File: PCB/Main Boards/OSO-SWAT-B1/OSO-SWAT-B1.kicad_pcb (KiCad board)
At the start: 2 copper layers, 24.4 x 24.4 mm, 37 parts, among them J1 OSO_SWD, U1 ATSAML22J18A-MUT, U2 MIC5365-3.3YC5-TR, X1 32.768 kHz, 12.5 pF

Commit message: as sent to JLCPCB 10/12
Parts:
- R1: value TBD -> 1K

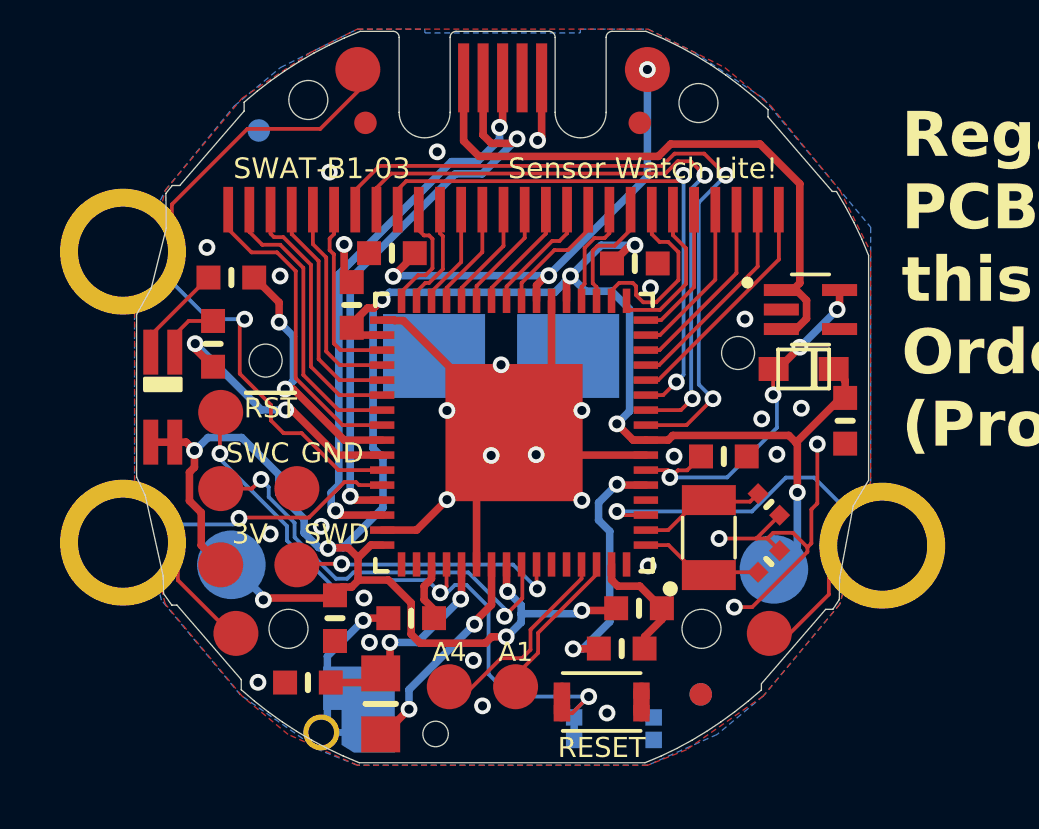
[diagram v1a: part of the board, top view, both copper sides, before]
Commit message: DFM changes for JLC release
- Change small value capacitors to 0.1uF
- Fix footprint / library associations
- Change test points to discrete footprints
- Use smaller LED
- Change to DFN-6 LDO
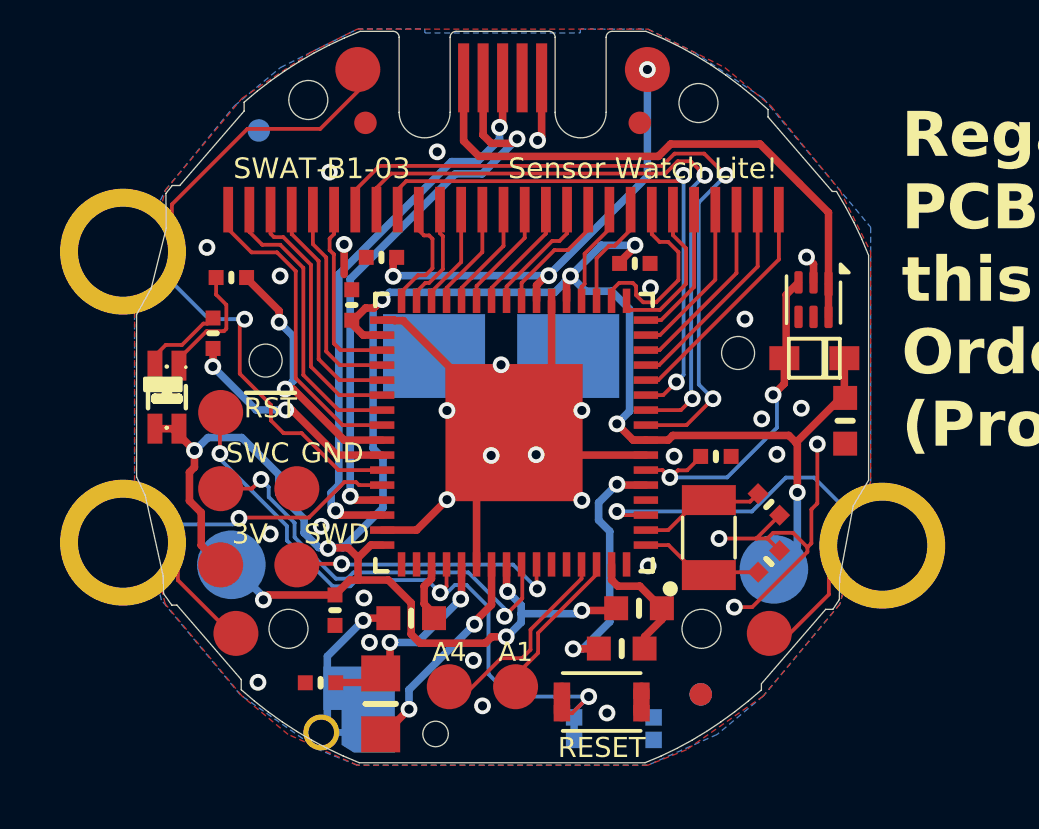
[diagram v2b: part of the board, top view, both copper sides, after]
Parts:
- removed J1: OSO_SWD, OSO-SWD:OSO_SWD_2x3
- removed U$5: , OSO-SWAT-A1-05:OSO_BEAR_250X360MIL_1000DPI
- removed U$6: , OSO-SWAT-A1-05:OSO_WORDMARK_ONELINE_350MIL_1000DPI
- removed U2: MIC5365-3.3YC5-TR, OSO-SWAT-A1-05:SOT65P210X110-5N
- added TP11: TestPoint, TestPoint:TestPoint_Pad_D1.5mm, F.Cu at (5.57, 13.3)
- added TP2: TestPoint, TestPoint:TestPoint_Pad_D1.5mm, F.Cu at (8.11, 18.4)
- added TP3: TestPoint, TestPoint:TestPoint_Pad_D1.5mm, F.Cu at (8.11, 15.9)
- added TP4: TestPoint, TestPoint:TestPoint_Pad_D1.5mm, F.Cu at (5.57, 18.4)
- added TP5: TestPoint, TestPoint:TestPoint_Pad_D1.5mm, F.Cu at (5.57, 15.9)
- added U3: TLV70033_WSON6, Package_SON:WSON-6_1.5x1.5mm_P0.5mm, F.Cu at (25.3, 9.56)
- C2, C3, C4, C5, C6, C9, R6, R7: footprint OSO-SWAT-A1-05:_0603MP -> OSO-SWAT-A1-05:_0402MP
- D2: renamed from LED0; value QBLP655-RIG -> XL-2012SURUGC; footprint OSO-SWAT-A1-05:LED_QBLP655 -> OSO-SWAT-A1-05:LED-SMD_4P-L2.0-W1.3-RD-TL
- TP1, TP10, TP6, TP7, TP8, TP9: value MICROBUILDER_TESTPOINTROUND1.5MM -> TestPoint; footprint OSO-SWAT-A1-05:MICROBUILDER_TESTPOINT_ROUND_1.5MM -> TestPoint:TestPoint_Pad_D1.5mm
- moved D1 0.51 mm to (25.4, 11.5)
- moved C5 0.42 mm to (8.90, 22.3)
- moved C6 0.38 mm to (10.9, 8.15)
- moved R6 0.35 mm to (5.32, 10.7)
- moved C9 0.27 mm to (22.1, 14.8)
- moved C2 0.27 mm to (9.38, 19.9)
- moved D2 0.14 mm to (3.78, 12.8), turned to -90 degrees
- renumbered RESET0 to SW0, RESET1 to SW1
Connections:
- D2 pad 1: VCC -> Net-(D2A-C)
- D2 pad 2: Net-(LED0A-C) -> VCC
- D2 pad 3: VCC -> Net-(D2B-C)
- D2 pad 4: Net-(LED0B-C) -> VCC
- R6 pad 2: Net-(LED0B-C) -> Net-(D2B-C)
- R7 pad 2: Net-(LED0A-C) -> Net-(D2A-C)
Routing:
- net Net-(D2A-C): track 0.00 -> 4.07 mm
- net Net-(LED0A-C): track 3.98 -> 0.00 mm
- net Net-(D2B-C): track 0.00 -> 2.79 mm
- net Net-(LED0B-C): track 2.04 -> 0.00 mm
- net /~{GREEN}: track 8.79 -> 7.34 mm
- net VBUS: track 20.4 -> 19.1 mm
- net +3V3: track 12.5 -> 11.9 mm, vias 4 -> 2
- net GND: track 36.7 -> 37.3 mm, vias 31 -> 32

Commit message: nudged test points further apart;  testjigulated
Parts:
- moved TP6 0.10 mm to (13.1, 22.5)
- moved TP7 0.10 mm to (15.5, 22.5)
- moved TP9 0.09 mm to (6.09, 20.8)
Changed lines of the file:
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@@
 				(font
 					(size 1.27 1.27)
+					(thickness 0.15)
 				)
 			)
@@
 	(footprint "TestPoint:TestPoint_Pad_D1.5mm"
 		(layer "F.Cu")
-		(at 13.1913 22.4616 180)
+		(at 13.0913 22.4616 180)
 		(descr "SMD pad as test Point, diameter 1.5mm")
 		(tags "test point SMD pad")
@@
 				(font
 					(size 1.27 1.27)
+					(thickness 0.15)
 				)
 			)
@@
 	(footprint "TestPoint:TestPoint_Pad_D1.5mm"
 		(layer "F.Cu")
-		(at 15.4011 22.4616 180)
+		(at 15.5011 22.4616 180)
 		(descr "SMD pad as test Point, diameter 1.5mm")
 		(tags "test point SMD pad")
@@
 	(footprint "TestPoint:TestPoint_Pad_D1.5mm"
 		(layer "F.Cu")
-		(at 6.0793 20.6836 180)
+		(at 6.09 20.77 180)
 		(descr "SMD pad as test Point, diameter 1.5mm")
 		(tags "test point SMD pad")
@@
 				(font
 					(size 1.27 1.27)
+					(thickness 0.15)
 				)
 			)
@@
 	)
 	(segment
+		(start 5.76 9.73)
+		(end 5.76 10.53)
+		(width 0.127)
+		(layer "F.Cu")
+		(net "Net-(D2A-C)")
+	)
+	(segment
+		(start 5.4189 9.3889)
+		(end 5.76 9.73)
+		(width 0.127)
+		(layer "F.Cu")
+		(net "Net-(D2A-C)")
+	)
+	(segment
+		(start 5.6795 10.6105)
+		(end 5.0995 10.6105)
+		(width 0.127)
+		(layer "F.Cu")
+		(net "Net-(D2A-C)")
+	)
+	(segment
+		(start 5.4189 8.8218)
+		(end 5.4189 9.3889)
+		(width 0.127)
+		(layer "F.Cu")
+		(net "Net-(D2A-C)")
+	)
+	(segment
+		(start 5.76 10.53)
+		(end 5.6795 10.6105)
+		(width 0.127)
+		(layer "F.Cu")
+		(net "Net-(D2A-C)")
+	)
+	(segment
+		(start 5.0995 10.6105)
+		(end 4.18 11.53)
+		(width 0.127)
+		(layer "F.Cu")
+		(net "Net-(D2A-C)")
+	)
+	(segment
+		(start 4.18 11.53)
+		(end 4.18 11.7596)
+		(width 0.127)
+		(layer "F.Cu")
+		(net "Net-(D2A-C)")
+	)
+	(segment
+		(start 13.1913 22.5886)
+		(end 13.0913 22.4886)
+		(width 0.127)
+		(layer "F.Cu")
+		(net "/A4{slash}D1{slash}MISO")
+	)
+	(segment
 		(start 17.6003 18.8586)
 		(end 17.6003 18.3849)
@@
 	)
 	(segment
+		(start 15.618288 21.5096)
+		(end 15.898794 21.229094)
+		(width 0.127)
+		(layer "F.Cu")
+		(net "/A4{slash}D1{slash}MISO")
+	)
+	(segment
 		(start 15.898794 21.229094)
 		(end 15.898794 20.560106)
@@
 	)
 	(segment
-		(start 13.8403 22.5886)
-		(end 14.9193 21.5096)
+		(start 15.898794 20.560106)
+		(end 17.6003 18.8586)
 		(width 0.127)
 		(layer "F.Cu")
@@
 	)
 	(segment
-		(start 15.898794 20.560106)
-		(end 17.6003 18.8586)
+		(start 13.9673 22.4616)
+		(end 14.9193 21.5096)
 		(width 0.127)
 		(layer "F.Cu")
@@
 	)
 	(segment
-		(start 13.1913 22.5886)
-		(end 13.8403 22.5886)
+		(start 13.0913 22.4616)
+		(end 13.9673 22.4616)
 		(width 0.127)
 		(layer "F.Cu")
@@
 	)
 	(segment
-		(start 15.618288 21.5096)
-		(end 15.898794 21.229094)
+		(start 13.0913 22.4886)
+		(end 13.0913 22.4616)
 		(width 0.127)
 		(layer "F.Cu")
@@
 	)
 	(segment
+		(start 5.1308 10.3565)
+		(end 4.99429 10.3565)
+		(width 0.127)
+		(layer "F.Cu")
+		(net "Net-(D2B-C)")
+	)
+	(segment
+		(start 5.3173 10.17)
+		(end 5.1308 10.3565)
+		(width 0.127)
+		(layer "F.Cu")
+		(net "Net-(D2B-C)")
+	)
+	(segment
+		(start 3.7395 11.0691)
+		(end 3.38 11.4286)
+		(width 0.127)
+		(layer "F.Cu")
+		(net "Net-(D2B-C)")
+	)
+	(segment
+		(start 4.99429 10.3565)
+		(end 4.28169 11.0691)
+		(width 0.127)
+		(layer "F.Cu")
+		(net "Net-(D2B-C)")
+	)
+	(segment
+		(start 4.28169 11.0691)
+		(end 3.7395 11.0691)
+		(width 0.127)
+		(layer "F.Cu")
+		(net "Net-(D2B-C)")
+	)
+	(segment
+		(start 3.38 11.4286)
+		(end 3.38 11.7596)
+		(width 0.127)
+		(layer "F.Cu")
+		(net "Net-(D2B-C)")
+	)
+	(segment
 		(start 13.6003 19.5126)
 		(end 13.6003 18.3849)
@@
 	)
 	(segment
-		(start 5.9183 20.6836)
-		(end 6.0793 20.6836)
-		(width 0.127)
-		(layer "F.Cu")
-		(net "/MODE")
-	)
-	(segment
 		(start 8.513556 16.8228)
 		(end 6.2063 16.8228)
@@
 	)
 	(segment
-		(start 10.182943 15.7407)
-		(end 10.083943 15.6417)
+		(start 4.007813 18.004638)
+		(end 4.007813 18.773113)
 		(width 0.127)
 		(layer "F.Cu")
@@
 	)
 	(segment
-		(start 3.417473 17.414298)
-		(end 4.143821 18.140646)
+		(start 10.182943 15.7407)
+		(end 10.083943 15.6417)
 		(width 0.127)
 		(layer "F.Cu")
@@
 	)
 	(segment
-		(start 4.143821 18.909121)
-		(end 5.9183 20.6836)
+		(start 5.9183 20.6836)
+		(end 6.0793 20.6836)
 		(width 0.127)
 		(layer "F.Cu")
@@
 	)
 	(segment
-		(start 4.143821 18.140646)
-		(end 4.143821 18.909121)
+		(start 4.007813 18.773113)
+		(end 5.9183 20.6836)
 		(width 0.127)
 		(layer "F.Cu")
@@
 		(net "/MODE")
 	)
+	(segment
+		(start 3.417473 17.414298)
+		(end 4.007813 18.004638)
+		(width 0.127)
+		(layer "F.Cu")
+		(net "/MODE")
+	)
 	(via
 		(at 6.1809 16.8482)
@@
 		(net "/SWDIO")
 	)
-	(segment
-		(start 5.1308 10.3565)
-		(end 4.99429 10.3565)
-		(width 0.127)
-		(layer "F.Cu")
-		(net "Net-(D2B-C)")
-	)
-	(segment
-		(start 5.3173 10.17)
-		(end 5.1308 10.3565)
-		(width 0.127)
-		(layer "F.Cu")
-		(net "Net-(D2B-C)")
-	)
-	(segment
-		(start 3.7395 11.0691)
-		(end 3.38 11.4286)
-		(width 0.127)
-		(layer "F.Cu")
-		(net "Net-(D2B-C)")
-	)
-	(segment
-		(start 4.99429 10.3565)
-		(end 4.28169 11.0691)
-		(width 0.127)
-		(layer "F.Cu")
-		(net "Net-(D2B-C)")
-	)
-	(segment
-		(start 4.28169 11.0691)
-		(end 3.7395 11.0691)
-		(width 0.127)
-		(layer "F.Cu")
-		(net "Net-(D2B-C)")
-	)
-	(segment
-		(start 3.38 11.4286)
-		(end 3.38 11.7596)
-		(width 0.127)
-		(layer "F.Cu")
-		(net "Net-(D2B-C)")
-	)
-	(segment
-		(start 5.76 9.73)
-		(end 5.76 10.53)
-		(width 0.127)
-		(layer "F.Cu")
-		(net "Net-(D2A-C)")
-	)
-	(segment
-		(start 5.4189 9.3889)
-		(end 5.76 9.73)
-		(width 0.127)
-		(layer "F.Cu")
-		(net "Net-(D2A-C)")
-	)
-	(segment
-		(start 5.6795 10.6105)
-		(end 5.0995 10.6105)
-		(width 0.127)
-		(layer "F.Cu")
-		(net "Net-(D2A-C)")
-	)
-	(segment
-		(start 5.4189 8.8218)
-		(end 5.4189 9.3889)
-		(width 0.127)
-		(layer "F.Cu")
-		(net "Net-(D2A-C)")
-	)
-	(segment
-		(start 5.76 10.53)
-		(end 5.6795 10.6105)
-		(width 0.127)
-		(layer "F.Cu")
-		(net "Net-(D2A-C)")
-	)
-	(segment
-		(start 5.0995 10.6105)
-		(end 4.18 11.53)
-		(width 0.127)
-		(layer "F.Cu")
-		(net "Net-(D2A-C)")
-	)
-	(segment
-		(start 4.18 11.53)
-		(end 4.18 11.7596)
-		(width 0.127)
-		(layer "F.Cu")
-		(net "Net-(D2A-C)")
-	)
 	(zone
